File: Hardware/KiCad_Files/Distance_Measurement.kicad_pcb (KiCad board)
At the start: 2 copper layers, 116 x 64 mm, 12 parts, among them J1 Conn_01x04_Female, J2 Screw_Terminal_01x02, Q1 2N5109, U1 WeMos_D1_mini

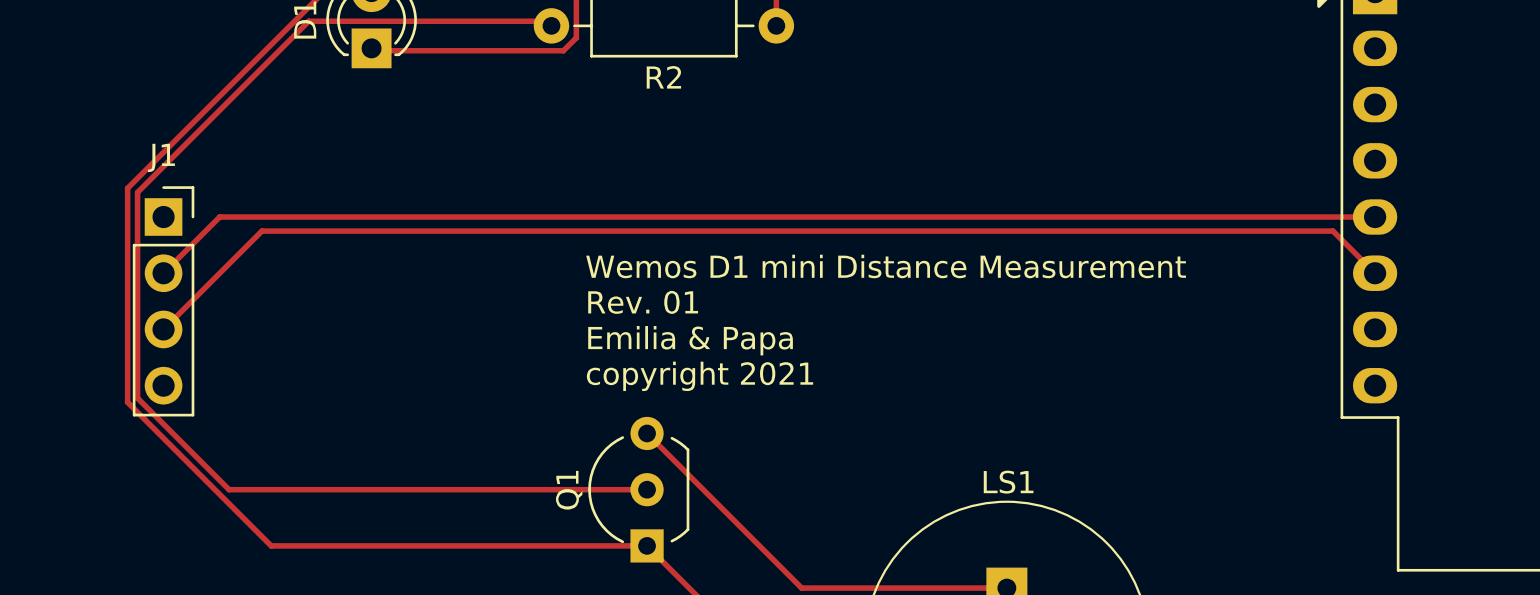
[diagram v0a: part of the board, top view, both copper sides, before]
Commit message: fixed a twisted GND/Vcc signal at PCB
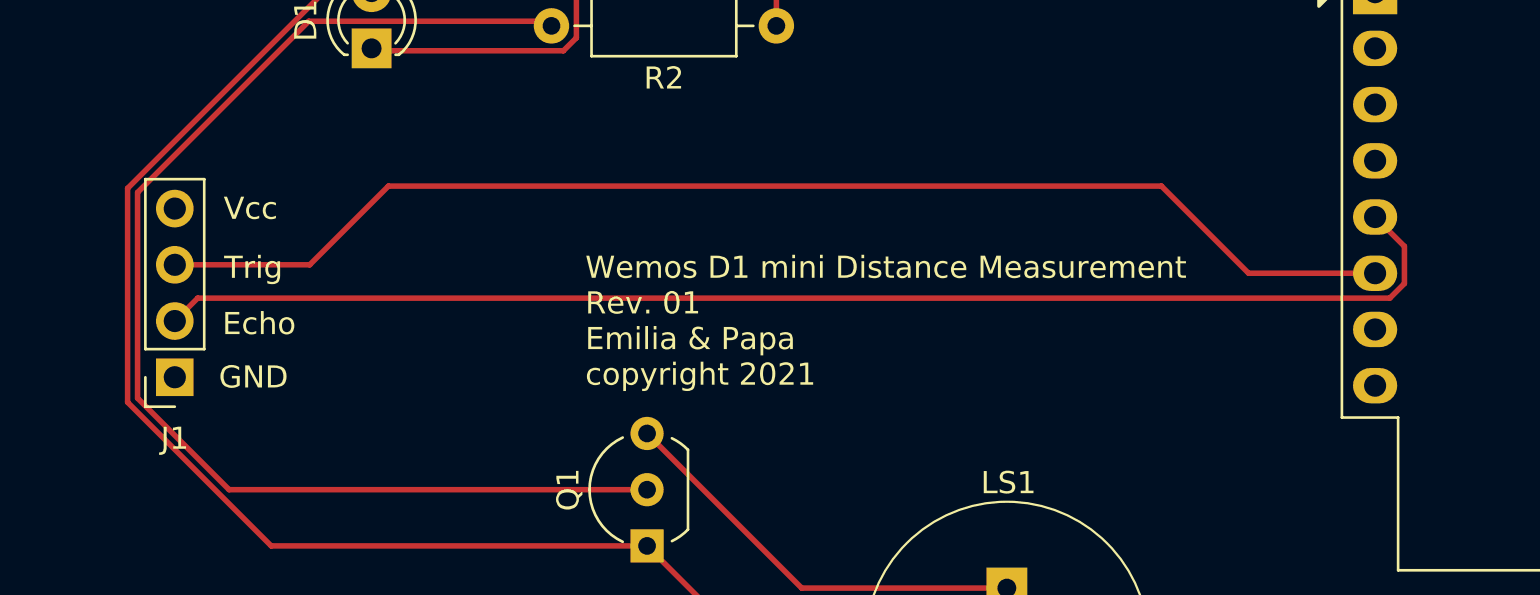
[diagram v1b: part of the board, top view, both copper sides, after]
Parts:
- moved J1 7.26 mm to (104.9, 104.0), turned to 180 degrees
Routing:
- net Net-(J1-Pad2): track 55.8 -> 59.8 mm
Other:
- board text added: "Echo"
- board text added: "Trig"
- board text added: "Vcc"

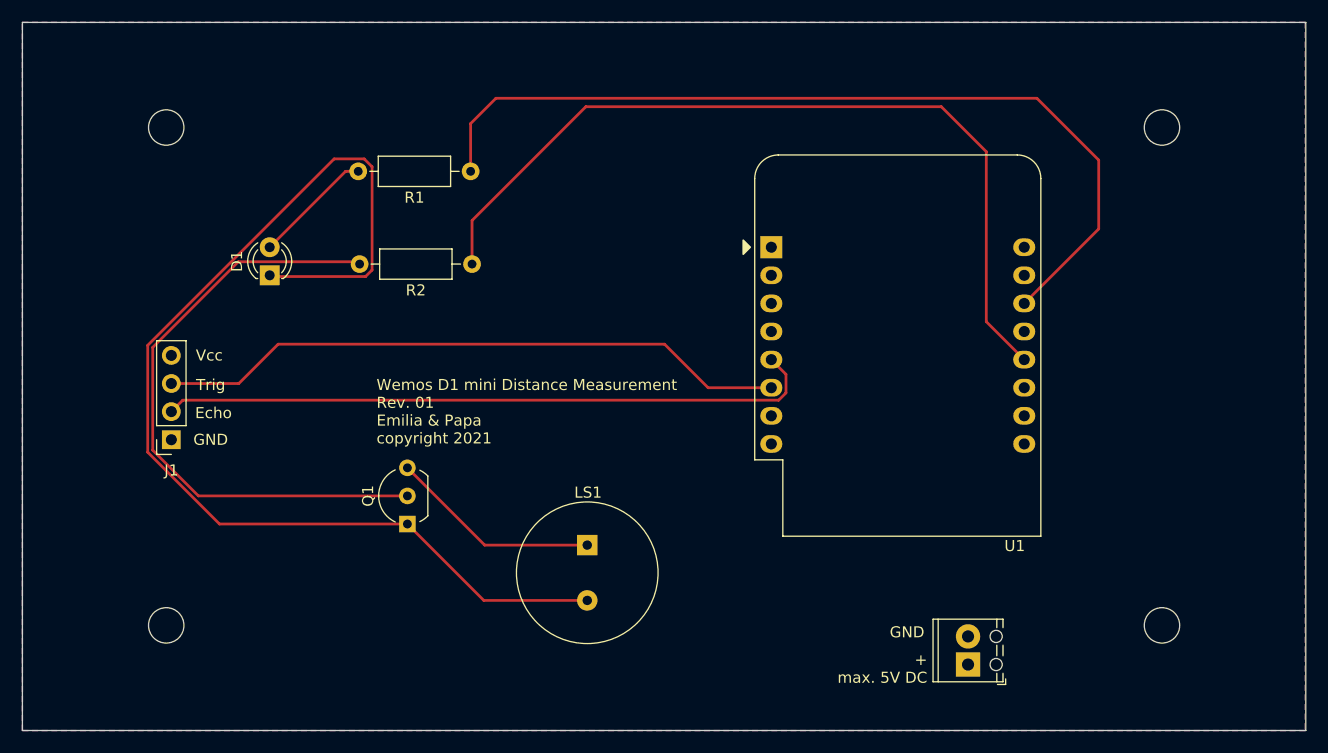
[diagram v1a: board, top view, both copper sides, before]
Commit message: corrected failure on PCB
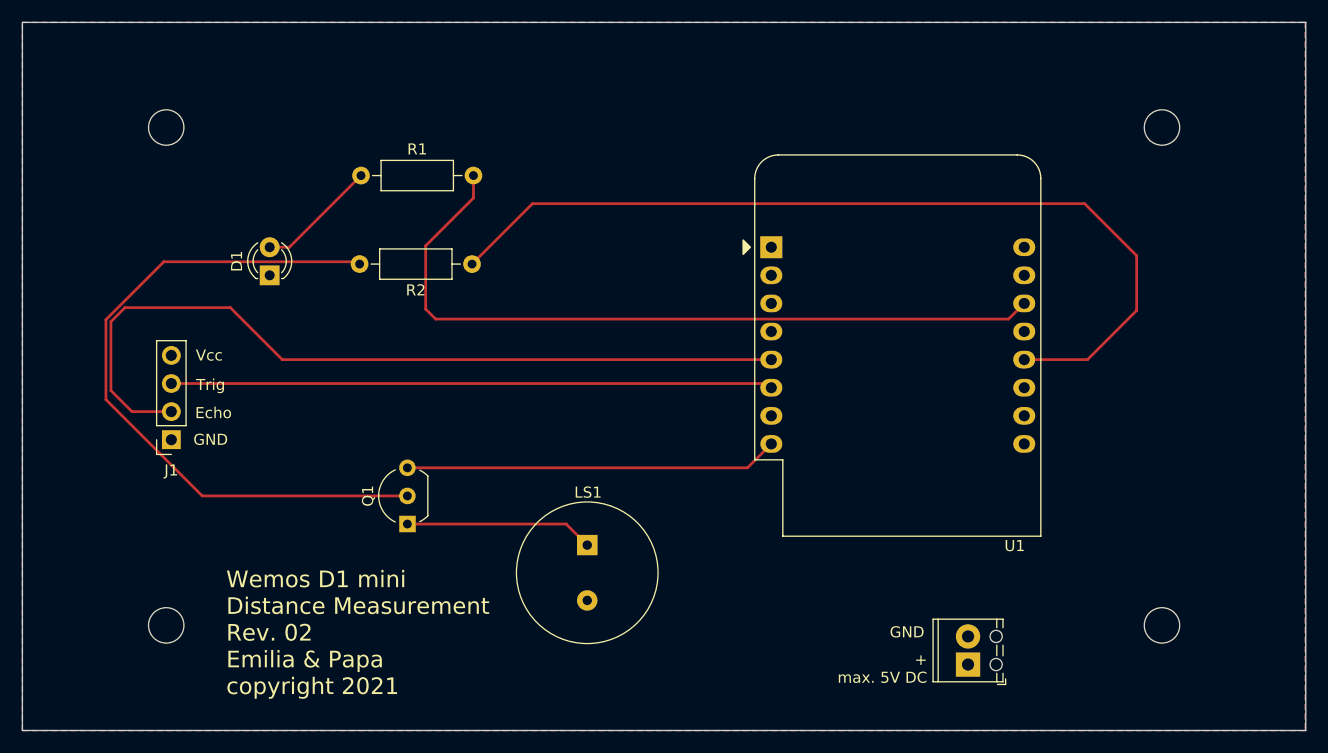
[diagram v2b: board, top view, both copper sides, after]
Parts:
- moved R1 9.91 mm to (122.0, 80.1), turned to 0 degrees
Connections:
- D1 pad 1: Net-(D1-Pad1) -> GND
- LS1 pad 2: Net-(D1-Pad1) -> GND
- Q1 pad 1: Net-(D1-Pad1) -> Net-(LS1-Pad1)
- Q1 pad 3: Net-(LS1-Pad1) -> Net-(Q1-Pad3)
- R1 pad 1: Net-(R1-Pad1) -> Net-(D1-Pad2)
- R1 pad 2: Net-(D1-Pad2) -> Net-(R1-Pad2)
- U1 pad 14: Net-(R1-Pad1) -> Net-(R1-Pad2)
- U1 pad 8: (no net) -> Net-(Q1-Pad3)
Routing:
- net Net-(D1-Pad1): track 101.4 -> 0.00 mm
- net Net-(R1-Pad1): track 80.1 -> 0.00 mm
- net Net-(R1-Pad2): track 0.00 -> 68.9 mm
- net Net-(Q1-Pad3): track 0.00 -> 33.8 mm
- net Net-(J1-Pad2): track 59.8 -> 74.6 mm
- net Net-(Q1-Pad2): track 56.0 -> 63.3 mm
- net Net-(R2-Pad1): track 76.6 -> 81.2 mm
- net Net-(J1-Pad3): track 57.3 -> 54.4 mm
- net Net-(LS1-Pad1): track 19.1 -> 17.0 mm
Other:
- board text added: "Wemos D1 mini Distance Measurement Rev. 02 Emilia & Papa copyright 2021"
- board text removed: "Wemos D1 mini Distance Measurement Rev. 01 Emilia & Papa copyright 2021"

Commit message: update of Gerber
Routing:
- net +5V: track 0.00 -> 83.9 mm
